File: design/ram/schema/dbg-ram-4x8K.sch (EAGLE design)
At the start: 45 parts

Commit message: Added initial schema for general purpose registers
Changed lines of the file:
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@@
 <?xml version="1.0" encoding="utf-8"?>
 <!DOCTYPE eagle SYSTEM "eagle.dtd">
-<eagle version="9.1.3">
+<eagle version="9.6.2">
 <drawing>
 <settings>
@@
 <plain>
 <text x="-27.94" y="1112.52" size="2.1844" layer="97">SRAM (STATIC RANDOM ACCESS MEMORY) 4x8K</text>
-<wire x1="-502.92" y1="1120.14" x2="-505.46" y2="871.22" width="0.1524" layer="97" style="shortdash"/>
-<wire x1="-505.46" y1="871.22" x2="48.26" y2="871.22" width="0.1524" layer="97" style="shortdash"/>
+<wire x1="-502.92" y1="1120.14" x2="-502.92" y2="871.22" width="0.1524" layer="97" style="shortdash"/>
+<wire x1="-502.92" y1="871.22" x2="48.26" y2="871.22" width="0.1524" layer="97" style="shortdash"/>
 <wire x1="48.26" y1="871.22" x2="48.26" y2="1120.14" width="0.1524" layer="97" style="shortdash"/>
 <wire x1="48.26" y1="1120.14" x2="-502.92" y2="1120.14" width="0.1524" layer="97" style="shortdash"/>
@@
 <attribute name="VALUE" x="-434.34" y="876.3" size="1.778" layer="96"/>
 </instance>
-<instance part="SW2" gate="G$1" x="-441.96" y="886.46" rot="R180"/>
+<instance part="SW2" gate="G$1" x="-441.96" y="886.46" smashed="yes" rot="R180">
+<attribute name="NAME" x="-436.88" y="883.285" size="1.778" layer="95" rot="R180"/>
+<attribute name="VALUE" x="-436.88" y="891.54" size="1.778" layer="96" rot="R180"/>
+</instance>
 <instance part="BUFFER-3" gate="A" x="-297.18" y="967.74" smashed="yes">
 <attribute name="NAME" x="-304.8" y="983.615" size="1.778" layer="95"/>

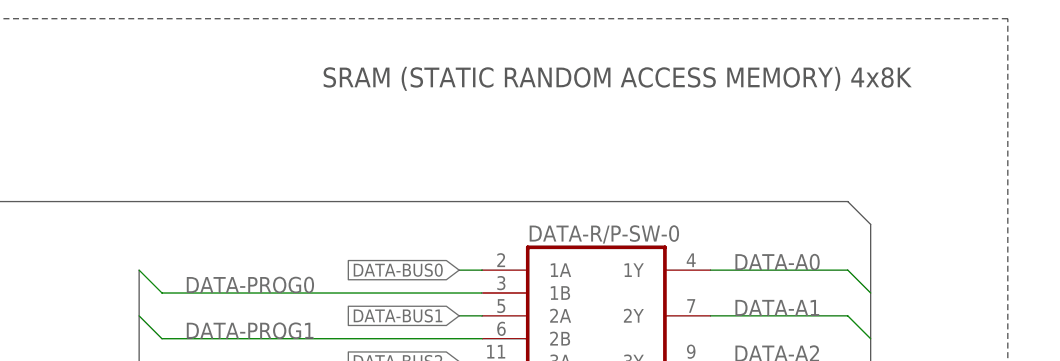
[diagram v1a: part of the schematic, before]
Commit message: Aligned titles size for all schemas
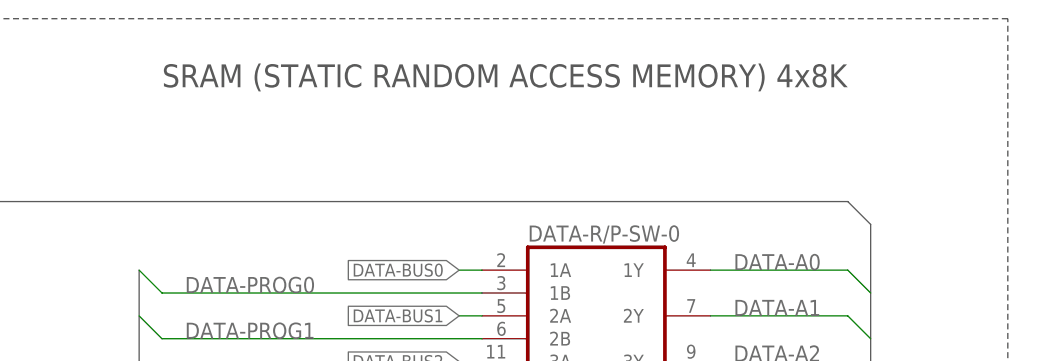
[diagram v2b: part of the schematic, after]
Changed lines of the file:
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@@
 <?xml version="1.0" encoding="utf-8"?>
 <!DOCTYPE eagle SYSTEM "eagle.dtd">
-<eagle version="9.6.2">
+<eagle version="9.1.3">
 <drawing>
 <settings>
@@
 <sheet>
 <plain>
-<text x="-27.94" y="1112.52" size="2.1844" layer="97">SRAM (STATIC RANDOM ACCESS MEMORY) 4x8K</text>
+<text x="-45.72" y="1112.52" size="2.54" layer="97">SRAM (STATIC RANDOM ACCESS MEMORY) 4x8K</text>
 <wire x1="-502.92" y1="1120.14" x2="-502.92" y2="871.22" width="0.1524" layer="97" style="shortdash"/>
 <wire x1="-502.92" y1="871.22" x2="48.26" y2="871.22" width="0.1524" layer="97" style="shortdash"/>

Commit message: Added separate reg for chip select of SRAM
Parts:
- added CHIP-SELECT-REG-0: 74LS173N, 74xx-eu:74LS173N
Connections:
- net ADDR-BUS10 renamed CS1
- net ADDR-BUS9 renamed CS0
- net PAGE-EN-A0 renamed CEN-A0
- net PAGE-EN-A1 renamed CEN-A1
- net PAGE-EN-A2 renamed CEN-A2
- net PAGE-EN-A3 renamed CEN-A3
- net PAGE-EN-B0 renamed CEN-B0
- net PAGE-EN-B1 renamed CEN-B1
- net PAGE-EN-B2 renamed CEN-B2
- net PAGE-EN-B3 renamed CEN-B3
- removed net ADDR-BUS8: ADDR-R/P-SW-2A.1A
- removed net ADDR-PAGE12: ADDR-R/P-SW-3A.1A, PAGE-ADDR-REG-0A.Q4
- new net ADDR-BUS12: ADDR-R/P-SW-3A.1A, CHIP-SELECT-REG-0A.Q3
- new net ADDR-PAGE8: ADDR-R/P-SW-2A.1A, PAGE-ADDR-REG-0A.Q1
- new net CS-EN: CHIP-SELECT-REG-0A.G1, CHIP-SELECT-REG-0A.G2
- new net N$1: CHIP-SELECT-REG-0A.Q1
- new net N$2: CHIP-SELECT-REG-0A.Q2
- net ADDR-PAGE10: now also PAGE-ADDR-REG-0A.Q3; no longer PAGE-ADDR-REG-0A.Q2
- net ADDR-PAGE11: now also PAGE-ADDR-REG-0A.Q4; no longer PAGE-ADDR-REG-0A.Q3
- net ADDR-PAGE9: now also PAGE-ADDR-REG-0A.Q2; no longer PAGE-ADDR-REG-0A.Q1
- net CLK-SIG: now also CHIP-SELECT-REG-0A.CLK
- net DATA-A4: now also CHIP-SELECT-REG-0A.D1
- net DATA-A5: now also CHIP-SELECT-REG-0A.D2
- net DATA-A6: now also CHIP-SELECT-REG-0A.D3
- net DATA-A7: now also CHIP-SELECT-REG-0A.D4
- net GND: now also CHIP-SELECT-REG-0A.CLR, CHIP-SELECT-REG-0A.M, CHIP-SELECT-REG-0A.N, CHIP-SELECT-REG-0A.Q4
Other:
- note added: "VER 1.6"
- moved on the sheet: PAGE-ADDR-REG-0
